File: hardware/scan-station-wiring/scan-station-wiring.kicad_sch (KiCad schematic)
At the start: 9 parts, among them J1 CYD SPI, J2 NFC Antenna Board, J4 NFC Antenna B, J6 Load Cell, U2 ADS1220IPWR, U3 AHT20, U4 PN5180A0HN, U5 AS7341-DLGM

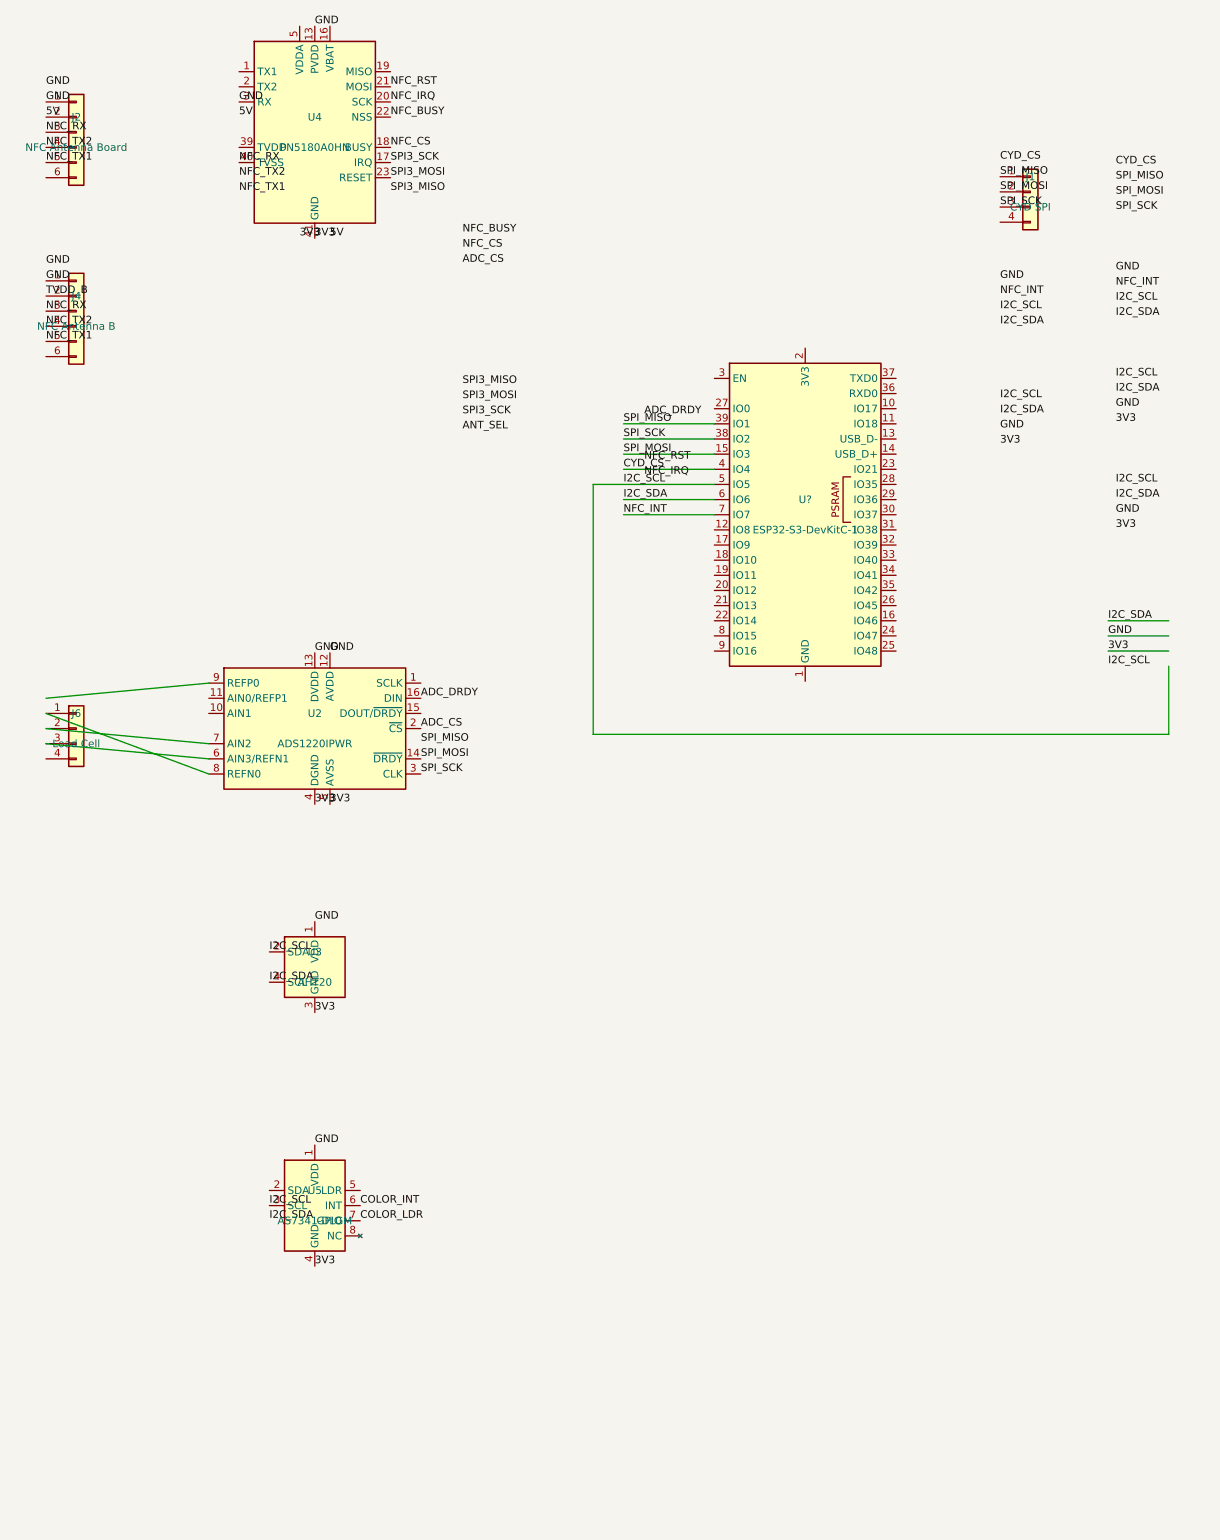
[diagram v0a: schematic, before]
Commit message: feat: add power supply, passives, and remaining components to schematic
- AMS1117-3.3 LDO regulator (5V→3.3V) with input/output caps
- USB-C power-only receptacle with CC1/CC2 5.1K pull-downs
- I2C pull-up resistors (4.7K on SDA/SCL)
- Decoupling caps (100nF) for ADS1220, AHT20, PN5180, AS7341
- Dual white LEDs with current limiting resistors for color sensor
  (transmissive + reflective measurement)
- TVDD switching MOSFETs for dual NFC antenna selection
- Second NFC antenna connector (antenna B)

Co-Authored-By: Claude Opus 4.6 (1M context) <noreply@anthropic.com>
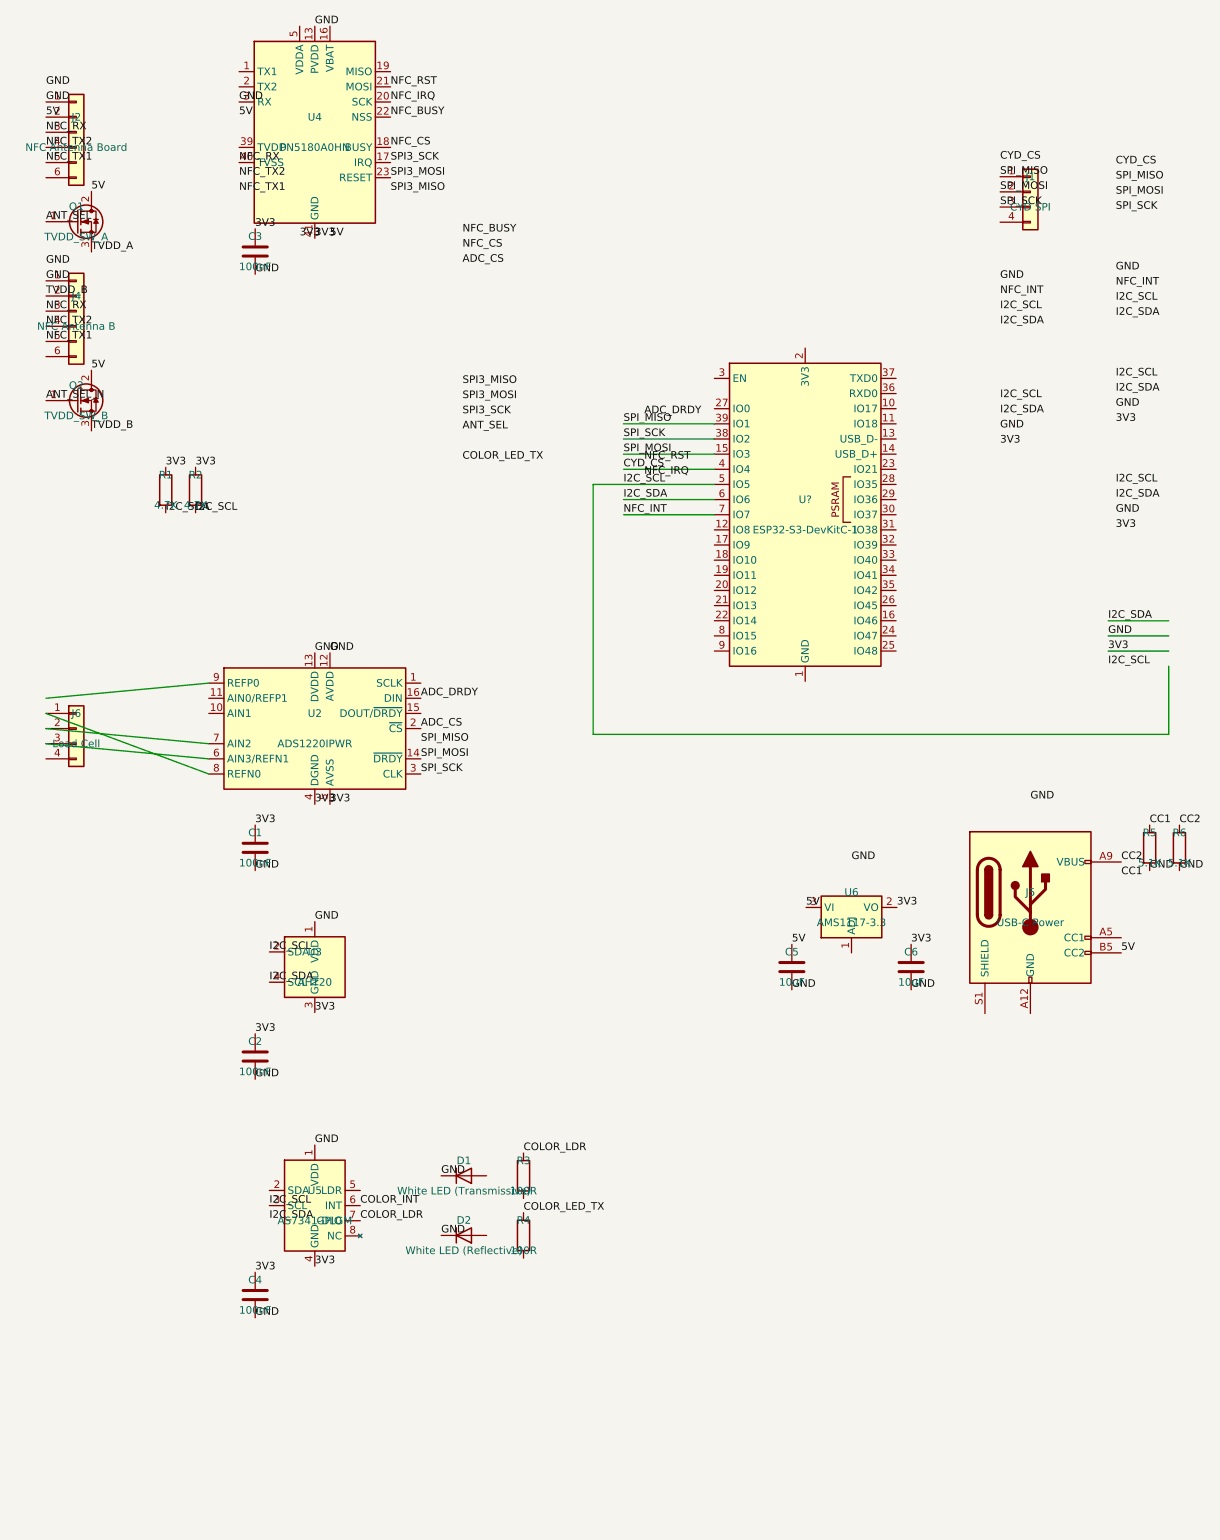
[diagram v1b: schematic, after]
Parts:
- added C1, C2, C3, C4: 100nF, symbol Device:C
- added C5, C6: 10uF, symbol Device:C
- added D1: White LED (Transmissive), symbol Device:LED
- added D2: White LED (Reflective), symbol Device:LED
- added J5: USB-C Power, symbol Connector:USB_C_Receptacle_PowerOnly_6P
- added Q1: TVDD_SW_A, symbol Transistor_FET:Q_NMOS_GDS
- added Q2: TVDD_SW_B, symbol Transistor_FET:Q_NMOS_GDS
- added R1, R2: 4.7K, symbol Device:R
- added R3, R4: 100R, symbol Device:R
- added R5, R6: 5.1K, symbol Device:R
- added U6: AMS1117-3.3, symbol Regulator_Linear:AMS1117
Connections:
- net 3V3: now also C1.1, C2.1, C3.1, C4.1, C6.1, R1.1, R2.1, U6.2 (VO)
- net 5V: now also C5.1, J5.B5 (CC2), Q1.2 (D), Q2.2 (D), U6.3 (VI)
- net ANT_SEL: now also Q1.1 (G)
- net COLOR_LDR: now also R3.1
- net GND: now also C1.2, C2.2, C3.2, C4.2, C5.2, C6.2, D1.1 (K), D2.1 (K), R5.2, R6.2
- net I2C_SCL: now also R2.2
- net I2C_SDA: now also R1.2
- net TVDD_B: now also Q2.3 (S)
- new net: J5.A12 (GND), J5.B12 (GND)
- new net ANT_SEL_N: Q2.1 (G)
- new net CC1: R5.1
- new net CC2: J5.A9 (VBUS), J5.B9 (VBUS), R6.1
- new net COLOR_LED_TX: R4.1
- new net TVDD_A: Q1.3 (S)

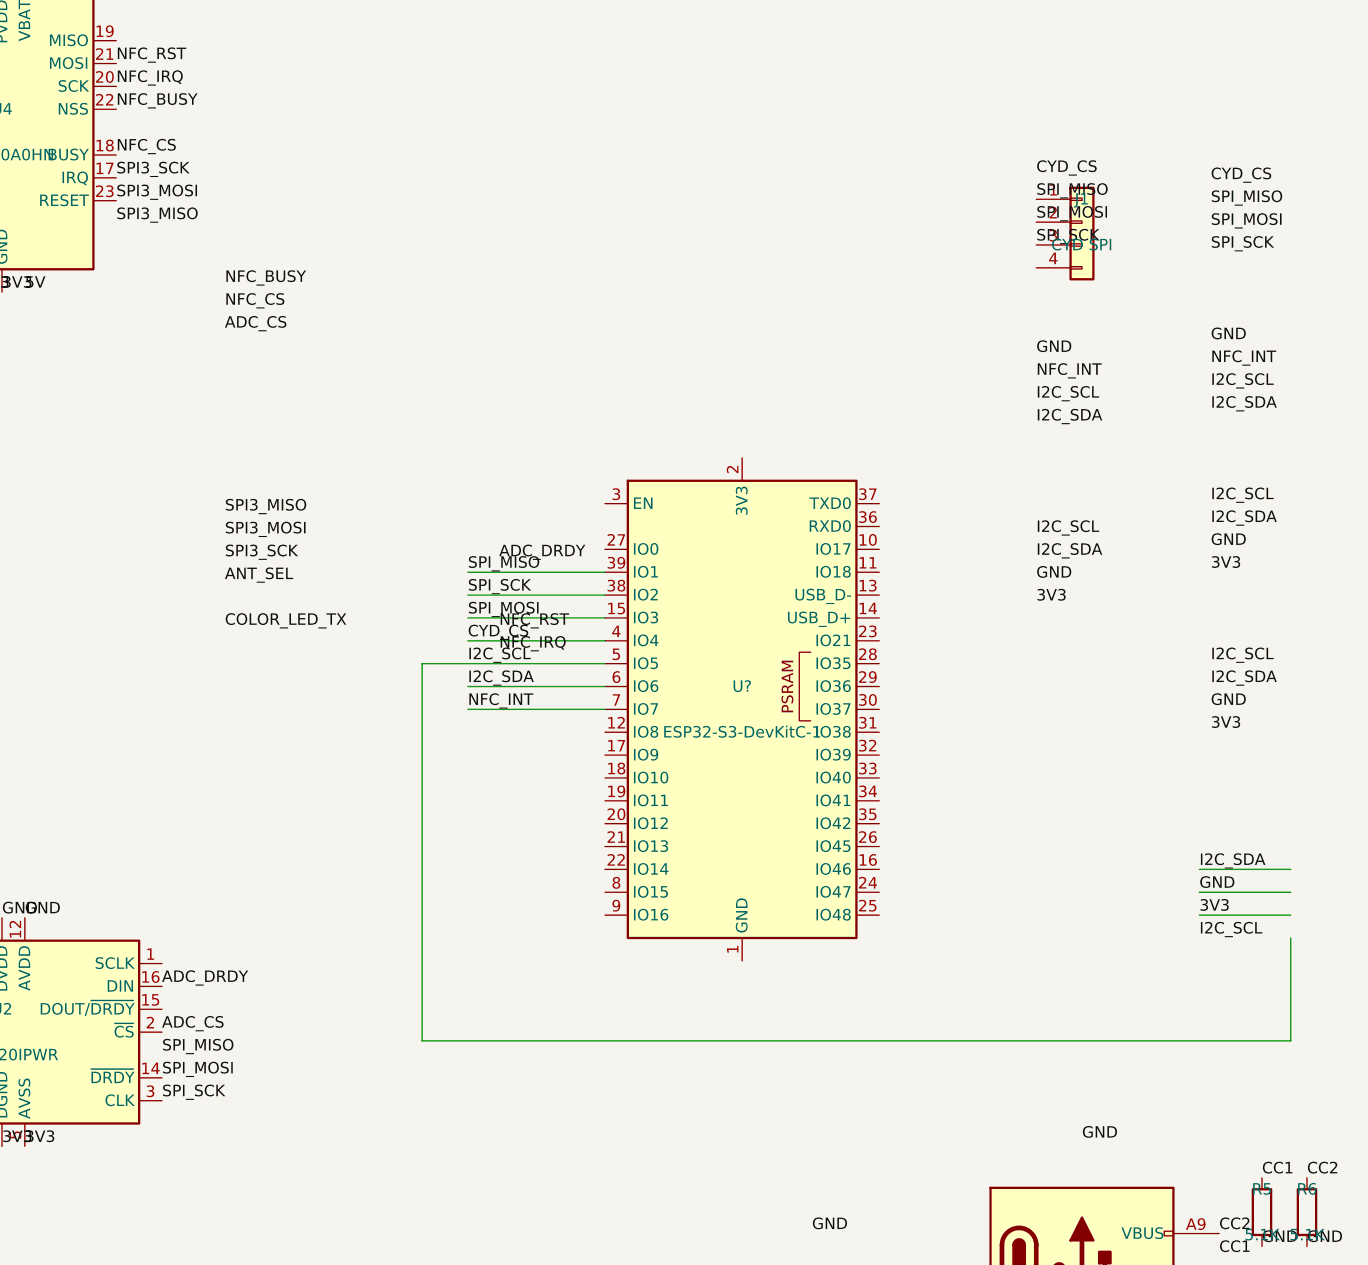
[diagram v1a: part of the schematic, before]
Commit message: chore: clean up carrier board schematic
- Pretty-print .kicad_sch file (was single line, now properly indented)
- Annotate U1 (ESP32-S3, was U?)
- Remove 29 orphaned net labels from deleted connectors
- Rename ADS1220 SPI labels: SPI_* → SPI3_* (shared sensor bus)
- Rename CYD SPI labels: SPI_* → SPI2_* (dedicated display bus)
- Remove stale NFC_INT label (replaced by PN5180 direct pins)

Co-Authored-By: Claude Opus 4.6 (1M context) <noreply@anthropic.com>
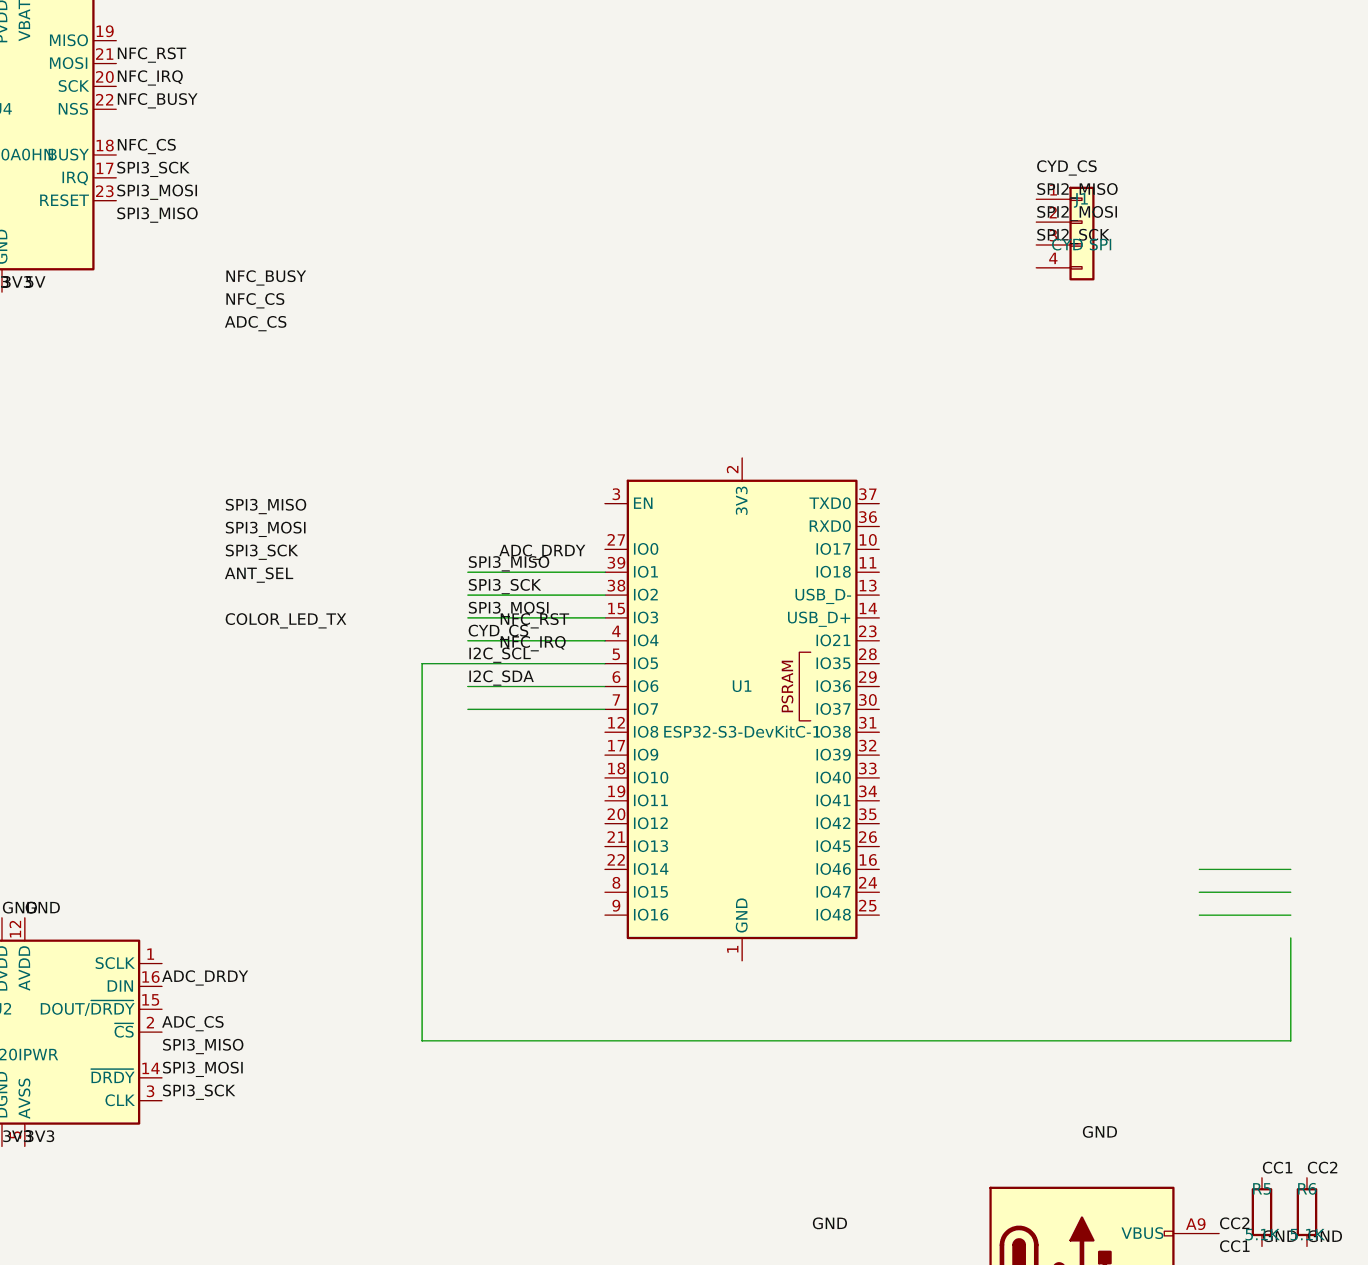
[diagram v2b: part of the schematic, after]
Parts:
- gave numbers to parts that had none: 1
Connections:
- net SPI3_MISO: now also U1.39 (IO1)
- net SPI3_MOSI: now also U1.15 (IO3), U2.14 (~{DRDY})
- net SPI3_SCK: now also U1.38 (IO2), U2.3 (CLK)
- net NFC_INT: no longer names the net of U1.7 (IO7)
- net SPI_MISO renamed SPI2_MISO
- net SPI2_MISO: no longer U1.39 (IO1)
- removed net SPI_MOSI: J1.2 (Pin_2), U1.15 (IO3), U2.14 (~{DRDY})
- removed net SPI_SCK: J1.3 (Pin_3), U1.38 (IO2), U2.3 (CLK)
- new net SPI2_MOSI: J1.2 (Pin_2)
- new net SPI2_SCK: J1.3 (Pin_3)
